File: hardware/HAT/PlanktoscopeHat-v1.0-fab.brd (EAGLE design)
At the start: 65 x 100 mm, 86 parts, among them J1 JUMPER-SMT_3_1-NC_PASTE_SILK, J2 JUMPER-SMT_3_1-NC_PASTE_SILK, J3 JUMPER-SMT_2_NC_PASTE_SILK, K1 SSQ-120-04-T-D, Q1 600mA/40V, Q2 DMG2305UX, Q3 DMP3013SFV-7, Q4 600mA/40V, U1 M24C32-WMN6, U2 LM36011YKBR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

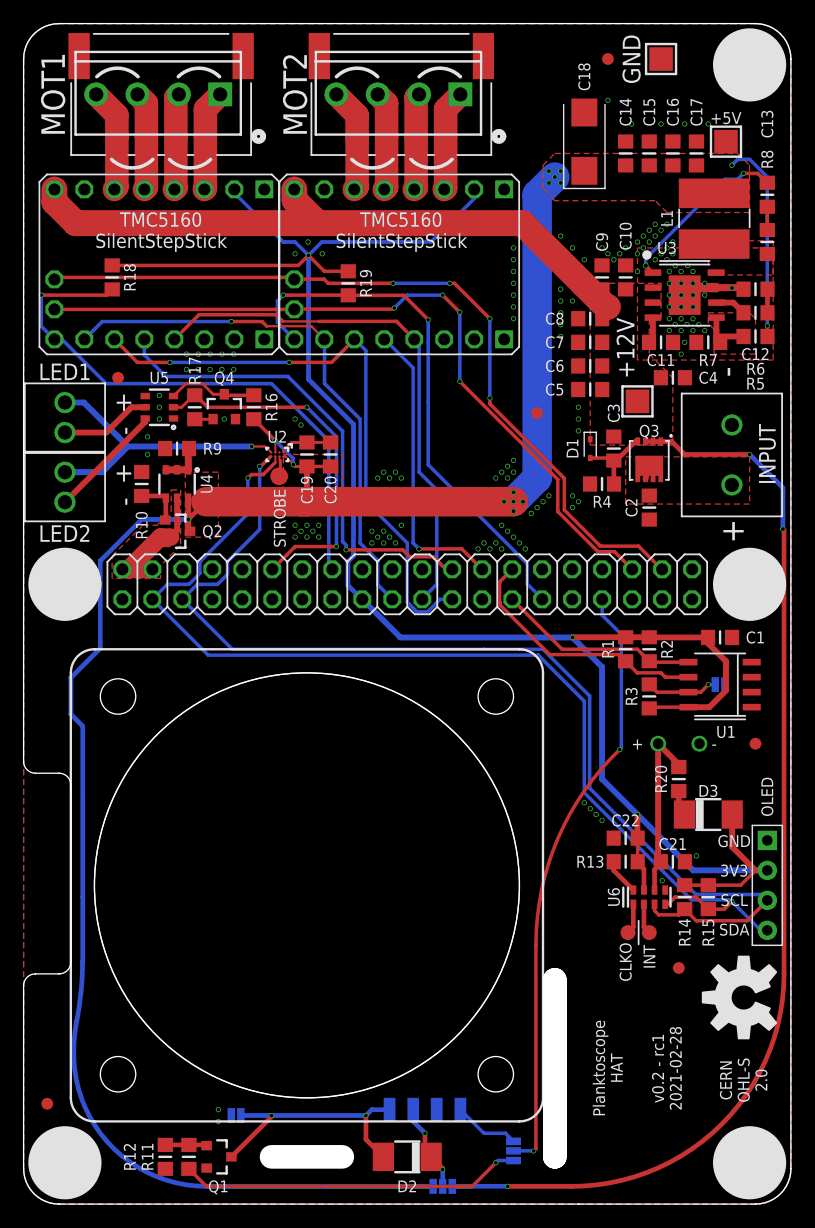
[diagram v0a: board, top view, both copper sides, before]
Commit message: hardware: hat fab files
(cherry picked from commit 8a2ba7d7322f03550dc010669ea8b1d036b7b47b)
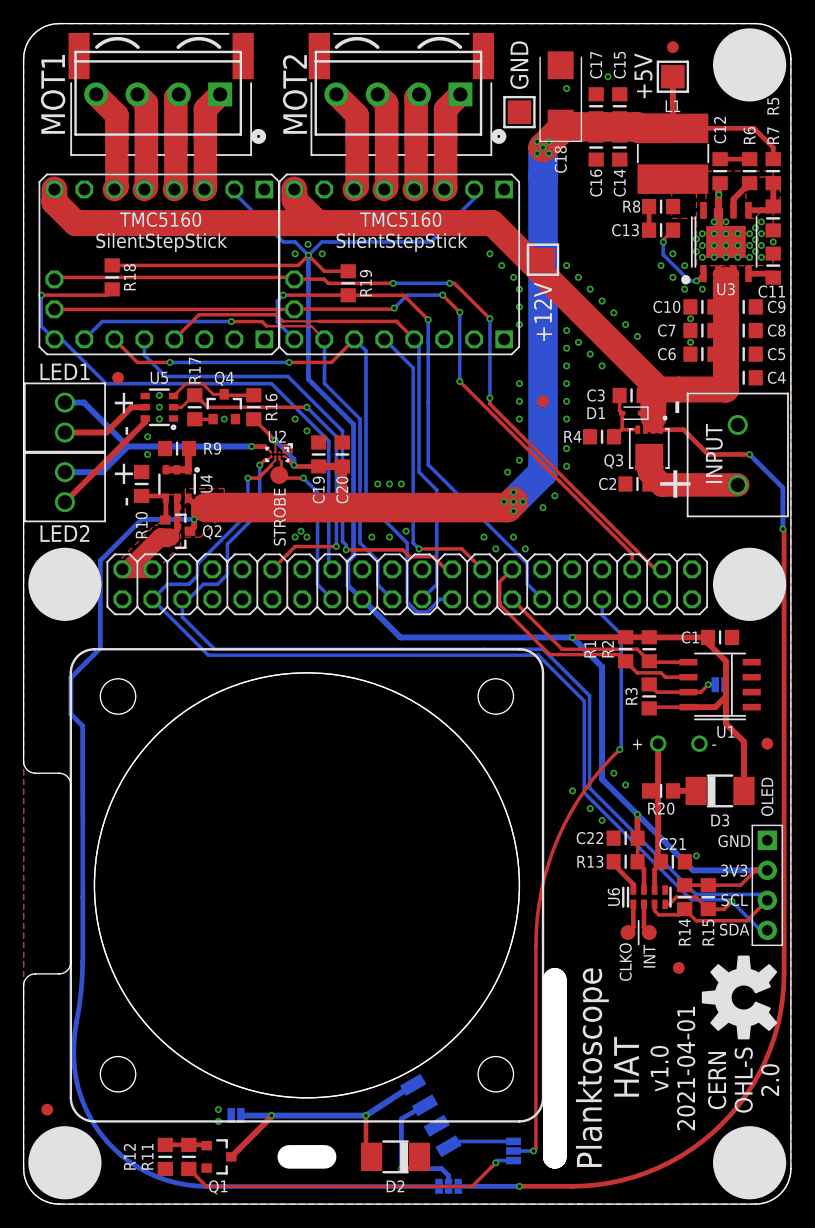
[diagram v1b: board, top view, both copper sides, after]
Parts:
- C19: value 10uF -> 100nF
- C20: value 100nF -> 10uF
- R11: value 10R -> 510R
- R12: value 1k -> 5.1k
- moved +12V 14.4 mm to (44.0, 80.0)
- moved R5 14.1 mm to (63.5, 87.5), turned to 90 degrees
- moved C5 13.3 mm to (61.0, 72.0), turned to 0 degrees
- moved C8 13.0 mm to (61.0, 74.0), turned to 0 degrees
- moved GND 12.8 mm to (42.0, 92.5)
- moved C9 12.3 mm to (61.0, 76.0), turned to 0 degrees
- moved R6 12.0 mm to (61.5, 87.5), turned to 270 degrees
- moved R7 11.9 mm to (63.5, 83.5), turned to 90 degrees
- moved C11 11.5 mm to (63.5, 79.5), turned to 90 degrees
- moved C12 10.4 mm to (59.0, 87.5), turned to 270 degrees
- moved C6 9.55 mm to (57.5, 72.0)
- moved C7 9.55 mm to (57.5, 74.0)
- moved C13 9.49 mm to (54.0, 82.5), turned to 0 degrees
- moved R8 9.49 mm to (54.0, 84.5), turned to 180 degrees
- moved C17 9.39 mm to (48.5, 93.0)
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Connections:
- removed net N$5: STROBE.TP, U2.B2
- net GPIO22: now also STROBE.TP, U2.B2
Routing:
- net +12V: track 145.3 -> 184.0 mm
- net +5V: track 181.8 -> 201.8 mm, vias 15 -> 13
- net VIN: track 1.17 -> 19.2 mm
- net GPIO22: track 0.00 -> 15.2 mm, vias 0 -> 1
- net BST: track 15.1 -> 7.02 mm
- net N$16: track 7.54 -> 13.9 mm, vias 2 -> 1
- net +3V3: track 170.8 -> 174.1 mm
- net N$8: track 21.8 -> 24.0 mm
- net VBACKUP: track 15.4 -> 13.4 mm
- net GND: track 10.4 -> 8.59 mm, vias 148 -> 101
- net N$5: track 1.75 -> 0.00 mm
- net N$6: track 6.87 -> 5.25 mm
- net GPIO20: track 67.6 -> 66.0 mm
- net I2C1_SCL: track 92.6 -> 93.5 mm
- net GPIO16: track 64.1 -> 63.3 mm
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- removed copper zone on layer 1, net +12V
- removed copper zone on layer 1, net VIN
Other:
- board text added: "v1.0 2021-04-01"
- board text removed: "v0.2 - rc1 2021-02-28"
